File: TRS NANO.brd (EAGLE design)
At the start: 71.1 x 64.5 mm, 29 parts, among them M1 ARDUINO-NANO-3.0, Q5 BC548, Q6 BC548, Q7 BC548, Q8 BC548, T1 351, T2 LM35, T3 351, T41 351, T42 351

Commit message: PDFs
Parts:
- renumbered S1 to MIN, S2 to MAX

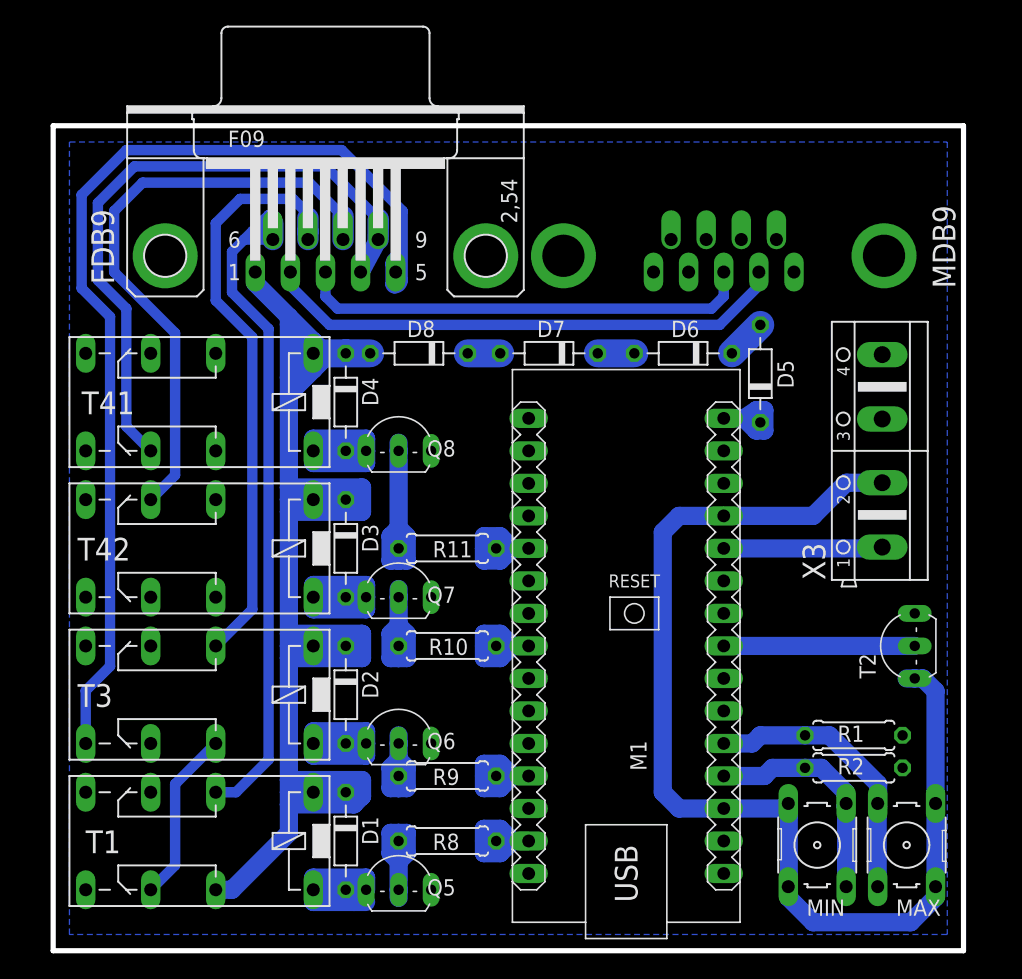
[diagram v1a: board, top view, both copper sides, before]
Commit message: elimina LM35
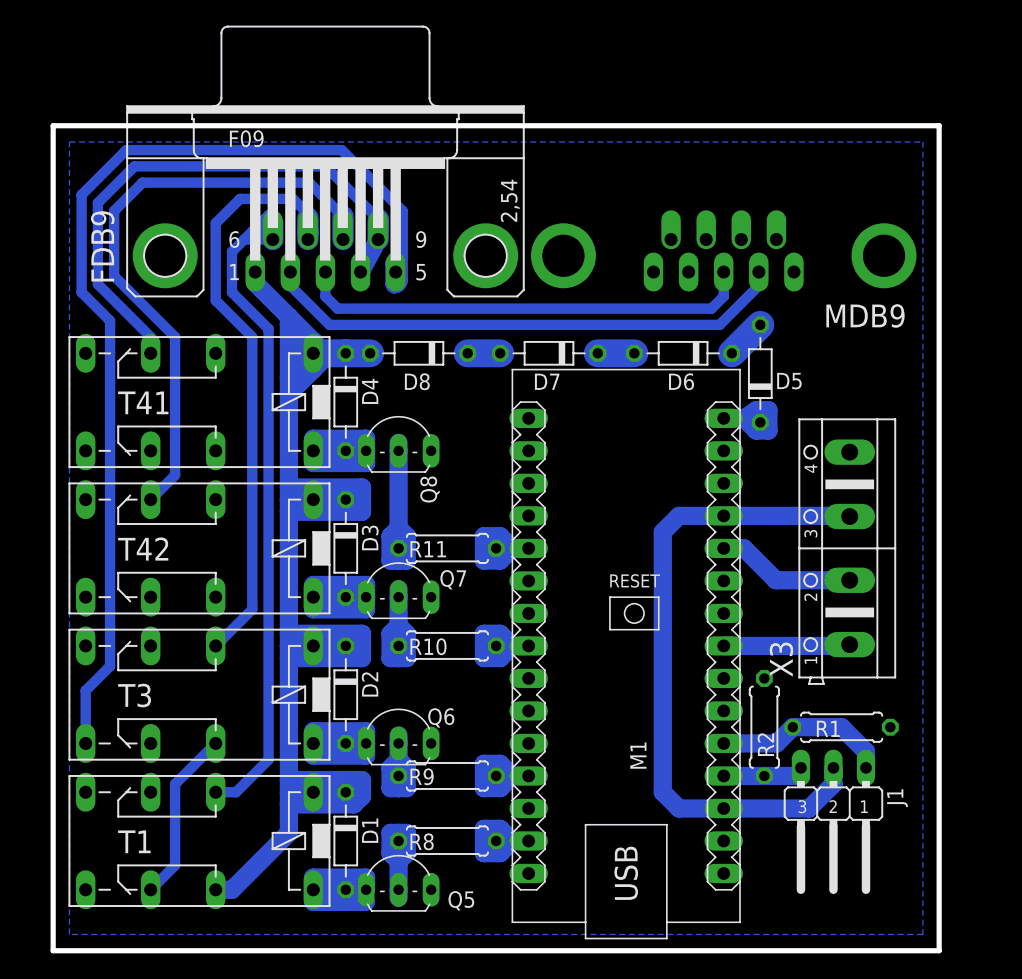
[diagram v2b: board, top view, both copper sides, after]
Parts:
- removed MAX, MIN: (no value), switch-omron:B3F-10XX
- removed T2: LM35, transistor-neu-to92:TO92-CBE
- added J1: (no value), jumper:JP2W
- moved X3 8.03 mm to (61.0, 30.2)
- moved R2 7.67 mm to (54.3, 16.2), turned to 90 degrees
- moved R1 1.14 mm to (60.3, 16.2), turned to 180 degrees
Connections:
- net +5V: now also J1.2, X3.3; no longer MAX.3, MAX.4, MIN.3, MIN.4, T2.C, X3.2
- net A0: now also J1.3; no longer MIN.1, MIN.2
- net A1: now also J1.1, R1.2; no longer MAX.1, MAX.2, R1.1
- net A4: now also X3.1; no longer T2.B
- net A7: now also X3.2; no longer X3.1
- net GND: now also R1.1, T41.O2; no longer R1.2, T2.E, T41.O1, X3.3
- net T41: now also T41.O1; no longer T41.O2
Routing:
- net +5V: track 89.8 -> 51.4 mm
- net A0: track 18.5 -> 6.67 mm
- net A1: track 22.5 -> 13.7 mm
- net T41: track 50.4 -> 42.7 mm
- net A4: track 14.9 -> 9.88 mm
- net A7: track 12.4 -> 10.9 mm
- net N$7: track 8.25 -> 8.88 mm
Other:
- board size 71.1 x 64.5 mm -> 69.2 x 64.5 mm

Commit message: atualiza placa
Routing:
- net TEMP: track 35.7 -> 35.0 mm
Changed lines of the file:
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@@
 <contactref element="FDB9" pad="3"/>
 <contactref element="MDB9" pad="3"/>
-<wire x1="20.955" y1="48.895" x2="50.165" y2="48.895" width="0.8128" layer="16"/>
-<wire x1="50.165" y1="48.895" x2="51.1175" y2="49.8475" width="0.8128" layer="16"/>
-<wire x1="51.1175" y1="49.8475" x2="51.1175" y2="51.7525" width="0.8128" layer="16"/>
-<wire x1="20.0025" y1="51.7525" x2="20.0025" y2="49.8475" width="0.8128" layer="16"/>
-<wire x1="20.0025" y1="49.8475" x2="20.955" y2="48.895" width="0.8128" layer="16"/>
+<wire x1="21.59" y1="48.895" x2="49.53" y2="48.895" width="0.8128" layer="16"/>
+<wire x1="49.53" y1="48.895" x2="51.1175" y2="50.4825" width="0.8128" layer="16"/>
+<wire x1="51.1175" y1="50.4825" x2="51.1175" y2="51.7525" width="0.8128" layer="16"/>
+<wire x1="20.0025" y1="51.7525" x2="20.0025" y2="50.4825" width="0.8128" layer="16"/>
+<wire x1="20.0025" y1="50.4825" x2="21.59" y2="48.895" width="0.8128" layer="16"/>
 </signal>
 <signal name="T41">
@@
 <contactref element="FDB9" pad="2"/>
 <contactref element="MDB9" pad="2"/>
-<wire x1="17.2593" y1="51.7525" x2="17.2593" y2="50.6857" width="0.8128" layer="16"/>
-<wire x1="17.2593" y1="50.6857" x2="20.32" y2="47.625" width="0.8128" layer="16"/>
-<wire x1="20.32" y1="47.625" x2="50.8" y2="47.625" width="0.8128" layer="16"/>
-<wire x1="53.8607" y1="51.7525" x2="53.8607" y2="50.6857" width="0.8128" layer="16"/>
-<wire x1="53.8607" y1="50.6857" x2="50.8" y2="47.625" width="0.8128" layer="16"/>
+<wire x1="17.2593" y1="51.7525" x2="17.2593" y2="51.0032" width="0.8128" layer="16"/>
+<wire x1="17.2593" y1="51.0032" x2="20.6375" y2="47.625" width="0.8128" layer="16"/>
+<wire x1="20.6375" y1="47.625" x2="50.4825" y2="47.625" width="0.8128" layer="16"/>
+<wire x1="53.8607" y1="51.7525" x2="53.8607" y2="51.0032" width="0.8128" layer="16"/>
+<wire x1="53.8607" y1="51.0032" x2="50.4825" y2="47.625" width="0.8128" layer="16"/>
 </signal>
 <signal name="N$10">

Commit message: update
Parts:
- removed X3: (no value), con-ptr500:AK500/4
- added IC: LM35, transistor-npn:TO92-EBC
- added R3: 500K, rcl:0207/7
- added R4: 1M, rcl:0207/15
- added SL2: (no value), con-amp-quick:03P
- added X1, X2: (no value), con-ptr500:AK500/2
- moved R2 7.96 mm to (54.9, 8.26), turned to 270 degrees
- moved D6 1.00 mm to (48.9, 45.1)
- moved J1 1.00 mm to (60.6, 11.4)
- moved M1 1.00 mm to (44.5, 22.2)
- moved R1 1.00 mm to (61.3, 15.9)
- moved D5 1.00 mm to (54.9, 43.5)
- moved D7 1.00 mm to (38.4, 45.1)
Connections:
- removed net A4: M1.J2.8, X3.1
- removed net A7: M1.J2.5, X3.2
- new net LM35_S: IC.B, M1.J2.6
- new net RX: M1.J1.1, SL2.1
- new net TEMP_S: M1.J2.5, R3.2, R4.1
- new net TRIM_A: M1.J2.8, X1.1
- new net TRIM_B: M1.J2.9, X1.2
- new net TX: M1.J1.2, SL2.2
- net +5V: now also IC.C, X2.2; no longer X3.3
- net GND: now also IC.E, R3.1, SL2.3, X2.1; no longer M1.J2.6, M1.J2.9, X3.4
- net TEMP: now also R4.2
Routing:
- net TEMP: track 35.0 -> 80.1 mm
- net TRIM_A: track 0.00 -> 21.7 mm
- net TRIM_B: track 0.00 -> 18.6 mm
- net +5V: track 51.4 -> 65.3 mm
- net A7: track 10.9 -> 0.00 mm
- net A4: track 9.88 -> 0.00 mm
- net LM35_S: track 0.00 -> 7.83 mm
- net TX: track 0.00 -> 5.41 mm
- net RX: track 0.00 -> 5.41 mm
- net D: track 10.6 -> 13.2 mm
- net C: track 10.6 -> 13.2 mm
- net B: track 10.6 -> 13.2 mm
- net A: track 10.6 -> 13.2 mm
- net N$16: track 2.54 -> 3.51 mm
- net N$7: track 8.88 -> 7.98 mm
- added copper zone on layer 16, net TEMP_S
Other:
- board size 69.2 x 64.5 mm -> 70.5 x 64.5 mm

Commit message: Add
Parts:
- removed SL2: (no value), con-amp-quick:03P
- added SV1: (no value), con-lstb:MA04-1
- R1: device rcl:0207/7 -> rcl:0207/10
- R10, R11, R8, R9: device rcl:0207/7 -> rcl:0207/5V
- moved R1 11.2 mm to (52.1, 9.53), turned to 90 degrees
- moved X2 5.54 mm to (62.9, 34.9)
- moved X1 5.54 mm to (62.9, 24.8)
- moved M1 3.18 mm to (41.3, 22.2)
- moved IC 2.86 mm to (54.6, 23.5)
- moved R3 2.54 mm to (52.4, 33.7)
- moved D6 1.62 mm to (47.3, 45.4)
- moved D5 1.62 mm to (53.3, 43.8)
- moved R4 1.59 mm to (55.9, 37.5)
- moved R11 1.31 mm to (28.3, 29.8), turned to 180 degrees
- moved R9 1.31 mm to (28.3, 12.1), turned to 180 degrees
- moved R8 1.31 mm to (28.3, 6.99), turned to 180 degrees
- moved R10 1.31 mm to (28.3, 22.2), turned to 180 degrees
- moved D7 1.00 mm to (37.5, 45.4)
- moved D8 0.32 mm to (27.6, 45.4)
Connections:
- net +5V: now also SV1.4
- net A: now also R8.1; no longer R8.2
- net B: now also R9.1; no longer R9.2
- net C: now also R10.1; no longer R10.2
- net D: now also R11.1; no longer R11.2
- net GND: now also SV1.3; no longer SL2.3
- net N$4: now also R9.2; no longer R9.1
- net N$5: now also R10.2; no longer R10.1
- net N$6: now also R11.2; no longer R11.1
- net N$8: now also R8.2; no longer R8.1
- net RX: now also SV1.1; no longer SL2.1
- net TX: now also SV1.2; no longer SL2.2
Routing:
- net C: track 13.2 -> 3.49 mm
- net B: track 13.2 -> 3.49 mm
- net A: track 13.2 -> 3.49 mm
- net D: track 13.2 -> 3.49 mm
- net N$8: track 11.3 -> 4.13 mm
- net N$5: track 12.3 -> 5.40 mm
- net N$6: track 16.1 -> 9.21 mm
- net +5V: track 65.3 -> 71.7 mm
- net N$4: track 10.4 -> 4.13 mm
- net TRIM_A: track 21.7 -> 17.4 mm
- net TEMP: track 80.1 -> 76.0 mm
- net TRIM_B: track 18.6 -> 15.0 mm
- net A0: track 6.67 -> 9.84 mm
- net A1: track 13.7 -> 16.6 mm
- net N$7: track 7.98 -> 5.08 mm
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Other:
- board size 70.5 x 64.5 mm -> 69.5 x 64.5 mm
